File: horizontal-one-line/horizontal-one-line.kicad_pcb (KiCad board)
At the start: 2 copper layers, 11 x 12.6 mm, 2 parts, among them J1 Grove-I2C-connector, J2 Conn_01x04

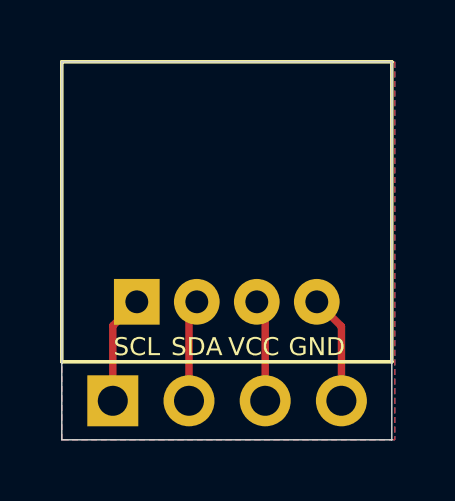
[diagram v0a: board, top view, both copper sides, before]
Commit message: Update silk lines for rev2021.02
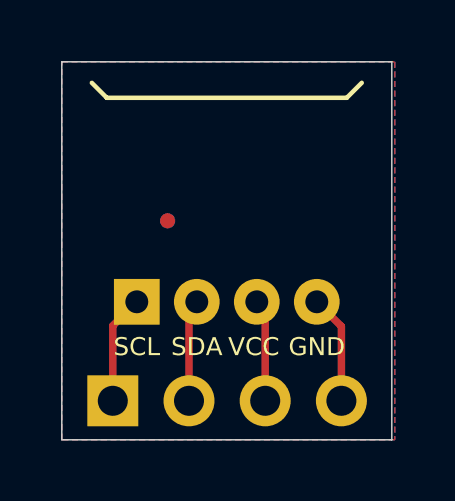
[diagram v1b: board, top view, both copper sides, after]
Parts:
- added fid1: Fiducial_0.5mm_Mask1mm, Fiducial:Fiducial_0.5mm_Mask1mm, B.Cu at (149.4, 74.4)
- added fid1: Fiducial_0.5mm_Mask1mm, Fiducial:Fiducial_0.5mm_Mask1mm, F.Cu at (149.4, 74.4)
- J1: footprint my-kicad-footprints:NS-Tech_Grove_1x04_P2mm_Horizontal -> my-kicad-footprints:NS-Tech_Grove_1x04_P2mm_Horizontal_silk_inside
- J2: footprint Connector_PinHeader_2.54mm:PinHeader_1x04_P2.54mm_Vertical -> my-kicad-footprints:PinHeader_1x04_P2.54mm_Vertical_silk_inside
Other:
- board text added: "Rev2021.02"
- board text removed: "Rev2020.12"
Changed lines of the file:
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@@
-(kicad_pcb (version 20171130) (host pcbnew 5.1.7-a382d34a8~87~ubuntu20.04.1)
+(kicad_pcb (version 20171130) (host pcbnew 5.1.9-73d0e3b20d~88~ubuntu20.04.1)
   (general
     (thickness 1.6)
@@
     (tracks 8)
     (zones 0)
-    (modules 2)
+    (modules 4)
     (nets 5)
   )
@@
     (add_net "Net-(J1-Pad3)")
   )
-  (module Connector_PinHeader_2.54mm:PinHeader_1x04_P2.54mm_Vertical (layer B.Cu)
+  (module Fiducial:Fiducial_0.5mm_Mask1mm (layer B.Cu)
+    (at 149.43 74.4)
+    (descr "Circular Fiducial, 0.5mm bare copper, 1mm soldermask opening (Level C)")
+    (tags fiducial)
+    (attr smd)
+    (fp_text reference fid1 (at 0 1.5) (layer B.SilkS) hide
+      (effects (font (size 1 1) (thickness 0.15)) (justify mirror))
+    )
+    (fp_text value Fiducial_0.5mm_Mask1mm (at 0 -1.5) (layer B.Fab) hide
+      (effects (font (size 1 1) (thickness 0.15)) (justify mirror))
+    )
+    (fp_circle (center 0 0) (end 0.5 0) (layer B.Fab) (width 0.1))
+    (fp_circle (center 0 0) (end 0.75 0) (layer B.CrtYd) (width 0.05))
+    (fp_text user %R (at 0 0) (layer B.Fab)
+      (effects (font (size 0.2 0.2) (thickness 0.04)) (justify mirror))
+    )
+    (pad "" smd circle (at 0 0) (size 0.5 0.5) (layers B.Cu B.Mask)
+      (solder_mask_margin 0.25) (clearance 0.25))
+  )
+  (module Fiducial:Fiducial_0.5mm_Mask1mm (layer F.Cu)
+    (at 149.425 74.4)
+    (descr "Circular Fiducial, 0.5mm bare copper, 1mm soldermask opening (Level C)")
+    (tags fiducial)
+    (attr smd)
+    (fp_text reference fid1 (at 0 -1.5) (layer F.SilkS) hide
+      (effects (font (size 1 1) (thickness 0.15)))
+    )
+    (fp_text value Fiducial_0.5mm_Mask1mm (at 0 1.5) (layer F.Fab) hide
+      (effects (font (size 1 1) (thickness 0.15)))
+    )
+    (fp_text user %R (at 0 0) (layer F.Fab)
+      (effects (font (size 0.2 0.2) (thickness 0.04)))
+    )
+    (fp_circle (center 0 0) (end 0.5 0) (layer F.Fab) (width 0.1))
+    (fp_circle (center 0 0) (end 0.75 0) (layer F.CrtYd) (width 0.05))
+    (pad "" smd circle (at 0 0) (size 0.5 0.5) (layers F.Cu F.Mask)
+      (solder_mask_margin 0.25) (clearance 0.25))
+  )
+  (module my-kicad-footprints:PinHeader_1x04_P2.54mm_Vertical_silk_inside (layer B.Cu)
     (at 147.6 80.4 270)
     (descr "Through hole straight pin header, 1x04, 2.54mm pitch, single row")
@@
       (effects (font (size 1 1) (thickness 0.15)) (justify mirror))
     )
+    (fp_text user %R (at 0 -3.81 180) (layer B.Fab)
+      (effects (font (size 1 1) (thickness 0.15)) (justify mirror))
+    )
     (fp_line (start 1.8 1.8) (end -1.8 1.8) (layer B.CrtYd) (width 0.05))
     (fp_line (start 1.8 -9.4) (end 1.8 1.8) (layer B.CrtYd) (width 0.05))
     (fp_line (start -1.8 -9.4) (end 1.8 -9.4) (layer B.CrtYd) (width 0.05))
     (fp_line (start -1.8 1.8) (end -1.8 -9.4) (layer B.CrtYd) (width 0.05))
-    (fp_line (start -1.33 1.33) (end 0 1.33) (layer B.SilkS) (width 0.12))
-    (fp_line (start -1.33 0) (end -1.33 1.33) (layer B.SilkS) (width 0.12))
-    (fp_line (start -1.33 -1.27) (end 1.33 -1.27) (layer B.SilkS) (width 0.12))
-    (fp_line (start 1.33 -1.27) (end 1.33 -8.95) (layer B.SilkS) (width 0.12))
-    (fp_line (start -1.33 -1.27) (end -1.33 -8.95) (layer B.SilkS) (width 0.12))
-    (fp_line (start -1.33 -8.95) (end 1.33 -8.95) (layer B.SilkS) (width 0.12))
+    (fp_line (start -1.03 1.03) (end 0.3 1.03) (layer B.SilkS) (width 0.12))
+    (fp_line (start -1.03 -0.3) (end -1.03 1.03) (layer B.SilkS) (width 0.12))
+    (fp_line (start -1.03 -8.65) (end 1.03 -8.65) (layer B.SilkS) (width 0.12))
     (fp_line (start -1.27 0.635) (end -0.635 1.27) (layer B.Fab) (width 0.1))
     (fp_line (start -1.27 -8.89) (end -1.27 0.635) (layer B.Fab) (width 0.1))
@@
     (fp_line (start 1.27 1.27) (end 1.27 -8.89) (layer B.Fab) (width 0.1))
     (fp_line (start -0.635 1.27) (end 1.27 1.27) (layer B.Fab) (width 0.1))
-    (fp_text user %R (at 0 -3.81 180) (layer B.Fab)
-      (effects (font (size 1 1) (thickness 0.15)) (justify mirror))
-    )
     (pad 4 thru_hole oval (at 0 -7.62 270) (size 1.7 1.7) (drill 1) (layers *.Cu *.Mask)
       (net 4 GND))
@@
     )
   )
-  (module my-kicad-footprints:NS-Tech_Grove_1x04_P2mm_Horizontal (layer F.Cu)
+  (module my-kicad-footprints:NS-Tech_Grove_1x04_P2mm_Horizontal_silk_inside (layer F.Cu)
     (at 151.4 77.1 90)
     (descr https://statics3.seeedstudio.com/images/opl/datasheet/3470130P1.pdf)
@@
       (effects (font (size 1 1) (thickness 0.15)))
     )
-    (fp_line (start -2 5.5) (end 8 5.5) (layer F.SilkS) (width 0.12))
-    (fp_line (start -2 -5.5) (end -2 5.5) (layer F.SilkS) (width 0.12))
-    (fp_line (start -2 -5.5) (end 8 -5.5) (layer F.SilkS) (width 0.12))
-    (fp_line (start 8 -5.5) (end 8 5.5) (layer F.SilkS) (width 0.12))
     (fp_text user %R (at -2 -1) (layer F.Fab)
       (effects (font (size 1 1) (thickness 0.15)))
     )
+    (fp_line (start 8 -5.5) (end 8 5.5) (layer F.Fab) (width 0.12))
+    (fp_line (start -2 -5.5) (end 8 -5.5) (layer F.Fab) (width 0.12))
+    (fp_line (start -2 -5.5) (end -2 5.5) (layer F.Fab) (width 0.12))
+    (fp_line (start -2 5.5) (end 8 5.5) (layer F.Fab) (width 0.12))
+    (fp_line (start 7.3 -4.5) (end 6.8 -4) (layer F.SilkS) (width 0.15))
+    (fp_line (start 6.8 -4) (end 6.8 4) (layer F.SilkS) (width 0.15))
+    (fp_line (start 6.8 4) (end 7.3 4.5) (layer F.SilkS) (width 0.15))
     (pad 4 thru_hole circle (at 0 3 90) (size 1.524 1.524) (drill 0.762) (layers *.Cu *.Mask)
       (net 4 GND))
@@
     (arrow2b (pts (xy 145.9 83.312) (xy 147.026504 82.725579)))
   )
-  (gr_text Rev2020.12 (at 153.3 74.3) (layer B.SilkS)
+  (gr_text Rev2021.02 (at 153.3 74.3) (layer B.SilkS)
     (effects (font (size 0.6 0.6) (thickness 0.15)) (justify mirror))
   )
